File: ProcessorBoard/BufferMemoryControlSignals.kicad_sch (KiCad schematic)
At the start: 4 parts, among them U1 74AHCT245

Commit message: ProcessorBoard: MEM no longer uses RDY signal
The open-drain RDY signal has been removed from the processor. Instead, the
process outputs /HLT to the system bus where it can be picked up by the
clock on the main board.

NOTE: This is a major difference between ProcessorBoard and MEMModule
right now.
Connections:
- net ~{RDY} renamed ~{AssertCtl}
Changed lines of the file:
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@@
     (effects (font (size 1.27 1.27)) (justify right))
   )
-  (hierarchical_label "~{RDY}" (shape input) (at 92.71 114.3 180) (fields_autoplaced)
+  (hierarchical_label "~{AssertCtl}" (shape input) (at 92.71 114.3 180) (fields_autoplaced)
     (effects (font (size 1.27 1.27)) (justify right))
   )

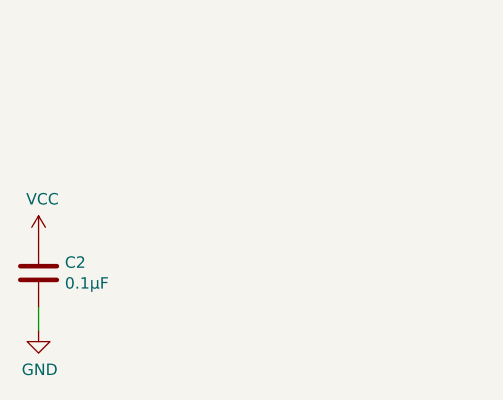
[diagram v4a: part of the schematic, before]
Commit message: ProcessorBoard: Replace µF with uF because some software gets confused.
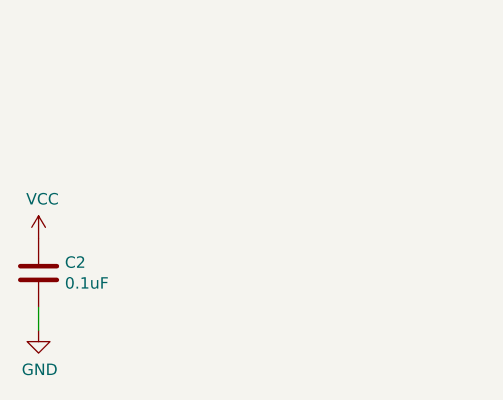
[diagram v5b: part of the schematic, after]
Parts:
- C2: value 0.1μF -> 0.1uF
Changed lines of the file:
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@@
       (effects (font (size 1.27 1.27)) (justify left))
     )
-    (property "Value" "0.1μF" (at 29.591 181.483 0)
+    (property "Value" "0.1uF" (at 29.591 181.483 0)
       (effects (font (size 1.27 1.27)) (justify left))
     )

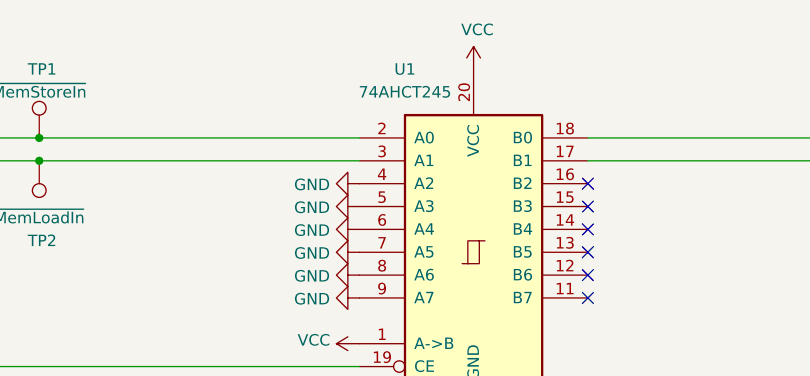
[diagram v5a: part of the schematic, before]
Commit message: ProcessorBoard: Use 74ABT where possible over 74AHCT
In several places, the schematics specify 74HC and 74AHCT versions of ICs
where choosing 74ABT would be fine, and would improve performance.
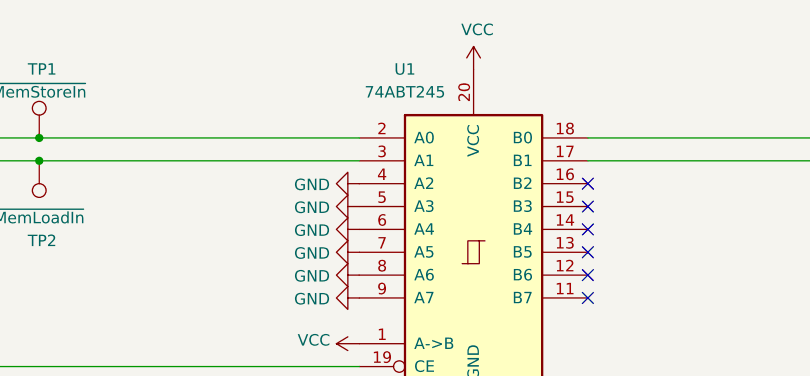
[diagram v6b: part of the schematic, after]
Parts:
- U1: value 74AHCT245 -> 74ABT245; Mouser https://www.mouser.com/ProductDetail/Nexperia/74AHCT245APWJ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 -> https://www.mouser.com/ProductDetail/Texas-Instruments/SN74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
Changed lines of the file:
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@@
       (effects (font (size 1.27 1.27)))
     )
-    (property "Value" "74AHCT245" (at 139.7 83.82 0)
+    (property "Value" "74ABT245" (at 139.7 83.82 0)
       (effects (font (size 1.27 1.27)))
     )
@@
       (effects (font (size 1.27 1.27)) hide)
     )
-    (property "Datasheet" "http://www.ti.com/lit/gpn/sn74LS245" (at 147.32 101.6 0)
+    (property "Datasheet" "https://www.ti.com/general/docs/suppproductinfo.tsp?distId=26&gotoUrl=https://www.ti.com/lit/gpn/sn74abt245b" (at 147.32 101.6 0)
       (effects (font (size 1.27 1.27)) hide)
     )
-    (property "Mouser" "https://www.mouser.com/ProductDetail/Nexperia/74AHCT245APWJ?qs=u4fy%2FsgLU9Nfcswc3zVmFw%3D%3D" (at 147.32 101.6 0)
+    (property "Mouser" "https://www.mouser.com/ProductDetail/Texas-Instruments/SN74ABT245BPWR?qs=5nGYs9Do7G2%2F7Vhs1ZTTgg%3D%3D" (at 147.32 101.6 0)
       (effects (font (size 1.27 1.27)) hide)
     )

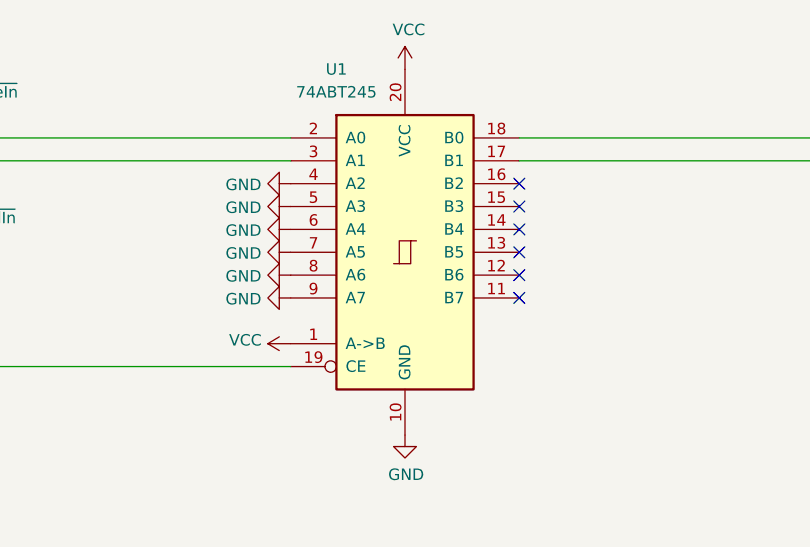
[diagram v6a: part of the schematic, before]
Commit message: ProcessorBoard: Copy symbols into project symbol library, make consistent
Symbols created for Turtle16 have been copied into a project-specific
symbol library. The symbols have all been updated with manufacturer,
manufacturer part number, mouser part number, and digikey part number.

Test points and mounting holes have been marked to be excluded from BOM.
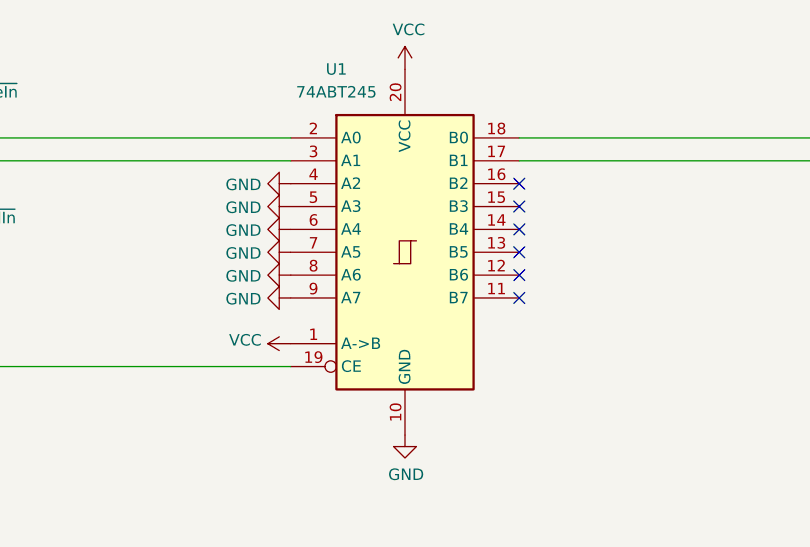
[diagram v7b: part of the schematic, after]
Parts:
- C2: footprint Capacitor_SMD:C_0603_1608Metric_Pad1.08x0.95mm_HandSolder -> Capacitor_SMD:C_0603_1608Metric; Digikey# (none) -> 587-6004-1-ND; Manufacturer (none) -> Taiyo Yuden; Manufacturer# (none) -> EMK107B7104KAHT; Mouser https://www.mouser.com/ProductDetail/963-EMK107B7104KAHT -> (none); Mouser# (none) -> 963-EMK107B7104KAHT
- TP1, TP2: now left out of the parts list
- U1: symbol 74xx:74LS245 -> Turtle16:74ABT245; Digikey# (none) -> 296-3971-1-ND; Manufacturer (none) -> Texas Instruments; Manufacturer# (none) -> SN74ABT245BPWR; Mouser https://www.mouser.com/ProductDetail/Texas-Instruments/SN74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 -> (none); Mouser# (none) -> 595-SN74ABT245BPWR
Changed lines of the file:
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@@
   (paper "USLetter")
   (title_block
-    (date "2023-11-20")
+    (date "2023-11-25")
     (rev "A")
   )
@@
       (effects (font (size 1.27 1.27)) (justify left))
     )
-    (property "Footprint" "Capacitor_SMD:C_0603_1608Metric_Pad1.08x0.95mm_HandSolder" (at 27.6352 184.15 0)
-      (effects (font (size 1.27 1.27)) hide)
-    )
-    (property "Datasheet" "~" (at 26.67 180.34 0)
-      (effects (font (size 1.27 1.27)) hide)
-    )
-    (property "Mouser" "https://www.mouser.com/ProductDetail/963-EMK107B7104KAHT" (at 26.67 180.34 0)
+    (property "Footprint" "Capacitor_SMD:C_0603_1608Metric" (at 128.5748 82.55 0)
+      (effects (font (size 1.27 1.27)) hide)
+    )
+    (property "Datasheet" "https://www.mouser.com/datasheet/2/396/taiyo_yuden_12132018_mlcc11_hq_e-1510082.pdf" (at 129.54 78.74 0)
+      (effects (font (size 1.27 1.27)) hide)
+    )
+    (property "Manufacturer" "Taiyo Yuden" (at 129.54 78.74 0)
+      (effects (font (size 1.27 1.27)) hide)
+    )
+    (property "Manufacturer#" "EMK107B7104KAHT" (at 129.54 78.74 0)
+      (effects (font (size 1.27 1.27)) hide)
+    )
+    (property "Mouser#" "963-EMK107B7104KAHT" (at 129.54 78.74 0)
+      (effects (font (size 1.27 1.27)) hide)
+    )
+    (property "Digikey#" "587-6004-1-ND" (at 129.54 78.74 0)
       (effects (font (size 1.27 1.27)) hide)
     )
@@
     )
   )
-  (symbol (lib_id "74xx:74LS245") (at 147.32 101.6 0) (unit 1)
+  (symbol (lib_id "Turtle16:74ABT245") (at 147.32 101.6 0) (unit 1)
     (in_bom yes) (on_board yes) (dnp no)
     (property "Reference" "U1" (at 139.7 81.28 0)
@@
       (effects (font (size 1.27 1.27)))
     )
-    (property "Footprint" "Package_SO:TSSOP-20_4.4x6.5mm_P0.65mm" (at 147.32 101.6 0)
-      (effects (font (size 1.27 1.27)) hide)
-    )
-    (property "Datasheet" "https://www.ti.com/general/docs/suppproductinfo.tsp?distId=26&gotoUrl=https://www.ti.com/lit/gpn/sn74abt245b" (at 147.32 101.6 0)
-      (effects (font (size 1.27 1.27)) hide)
-    )
-    (property "Mouser" "https://www.mouser.com/ProductDetail/Texas-Instruments/SN74ABT245BPWR?qs=5nGYs9Do7G2%2F7Vhs1ZTTgg%3D%3D" (at 147.32 101.6 0)
+    (property "Footprint" "Package_SO:TSSOP-20_4.4x6.5mm_P0.65mm" (at 147.32 99.06 0)
+      (effects (font (size 1.27 1.27)) hide)
+    )
+    (property "Datasheet" "https://www.ti.com/general/docs/suppproductinfo.tsp?distId=26&gotoUrl=https://www.ti.com/lit/gpn/sn74abt245b" (at 147.32 99.06 0)
+      (effects (font (size 1.27 1.27)) hide)
+    )
+    (property "Manufacturer" "Texas Instruments" (at 147.32 101.6 0)
+      (effects (font (size 1.27 1.27)) hide)
+    )
+    (property "Manufacturer#" "SN74ABT245BPWR" (at 147.32 101.6 0)
+      (effects (font (size 1.27 1.27)) hide)
+    )
+    (property "Mouser#" "595-SN74ABT245BPWR" (at 147.32 101.6 0)
+      (effects (font (size 1.27 1.27)) hide)
+    )
+    (property "Digikey#" "296-3971-1-ND" (at 147.32 101.6 0)
       (effects (font (size 1.27 1.27)) hide)
     )
@@
   )
   (symbol (lib_id "Connector:TestPoint") (at 99.06 91.44 0) (mirror x) (unit 1)
-    (in_bom yes) (on_board yes) (dnp no)
+    (in_bom no) (on_board yes) (dnp no)
     (property "Reference" "TP2" (at 97.79 100.33 0)
       (effects (font (size 1.27 1.27)) (justify left))
@@
   )
   (symbol (lib_id "Connector:TestPoint") (at 99.06 88.9 0) (unit 1)
-    (in_bom yes) (on_board yes) (dnp no)
+    (in_bom no) (on_board yes) (dnp no)
     (property "Reference" "TP1" (at 97.79 81.28 0)
       (effects (font (size 1.27 1.27)) (justify left))
